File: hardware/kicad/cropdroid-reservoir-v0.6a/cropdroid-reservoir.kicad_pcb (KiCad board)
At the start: 2 copper layers, 303.3 x 178.1 mm, 42 parts, among them J1 703W-00_52, J10 PJ-102A, J11 PJ-102A, J12 PJ-102A, J13 PJ-102A, J14 PJ-102A, J2 2172034-1, J3 2172034-1, J4 PJ-102A, J5 3-213598-2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

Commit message: fix broken board edge
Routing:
- net Net-(J2-Pad1): track 217.5 -> 218.3 mm
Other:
- outline, holes or cut-outs redrawn
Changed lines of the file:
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@@
   (general
     (thickness 1.6)
-    (drawings 23)
-    (tracks 279)
+    (drawings 25)
+    (tracks 280)
     (zones 0)
     (modules 42)
@@
   )
   (setup
-    (last_trace_width 0.762)
+    (last_trace_width 0.254)
     (user_trace_width 0.254)
     (user_trace_width 0.762)
@@
       (padsonsilk false)
       (subtractmaskfromsilk false)
-      (outputformat 3)
+      (outputformat 5)
       (mirror false)
       (drillshape 0)
@@
     )
   )
+  (gr_line (start 155.5242 158.1658) (end 155.5242 163.7538) (layer Edge.Cuts) (width 0.05))
+  (gr_line (start 155.5242 163.7538) (end 155.5242 158.1658) (layer F.SilkS) (width 0.12))
   (gr_line (start 155.5242 163.7538) (end 155.5242 214.0458) (layer Edge.Cuts) (width 0.05))
-  (gr_line (start 64.3382 163.7538) (end 155.5242 163.7538) (layer Edge.Cuts) (width 0.05))
+  (gr_line (start 64.3382 158.1658) (end 155.5242 158.1658) (layer Edge.Cuts) (width 0.05))
   (gr_text "+5V DC" (at 307.4162 143.6878) (layer F.SilkS)
     (effects (font (size 1 1) (thickness 0.15)))
@@
     (effects (font (size 1 1) (thickness 0.15)))
   )
-  (gr_line (start 64.3382 35.9918) (end 64.3382 163.7538) (layer Edge.Cuts) (width 0.05))
+  (gr_line (start 64.3382 35.9918) (end 64.3382 158.1658) (layer Edge.Cuts) (width 0.05))
   (gr_text "+12v DC" (at 291.9222 176.1998) (layer F.SilkS)
     (effects (font (size 1 1) (thickness 0.15)))
@@
   (segment (start 320.3702 209.2198) (end 321.1322 208.4578) (width 0.254) (layer F.Cu) (net 79))
   (segment (start 149.3012 151.9428) (end 143.2052 151.9428) (width 0.254) (layer F.Cu) (net 80))
-  (segment (start 156.784284 159.425884) (end 149.3012 151.9428) (width 0.254) (layer F.Cu) (net 80))
-  (segment (start 156.784284 209.575574) (end 156.784284 159.425884) (width 0.254) (layer F.Cu) (net 80))
+  (segment (start 303.2 207.04) (end 296.85421 213.38579) (width 0.254) (layer F.Cu) (net 80))
+  (segment (start 156.784284 209.575574) (end 156.784284 157.901884) (width 0.254) (layer F.Cu) (net 80))
   (segment (start 160.5945 213.38579) (end 156.784284 209.575574) (width 0.254) (layer F.Cu) (net 80))
+  (segment (start 156.784284 157.901884) (end 150.8252 151.9428) (width 0.254) (layer F.Cu) (net 80))
   (segment (start 296.85421 213.38579) (end 160.5945 213.38579) (width 0.254) (layer F.Cu) (net 80))
-  (segment (start 296.85421 213.38579) (end 303.2 207.04) (width 0.254) (layer F.Cu) (net 80))
+  (segment (start 150.8252 151.9428) (end 149.3012 151.9428) (width 0.254) (layer F.Cu) (net 80))
   (zone (net 1) (net_name GND) (layer F.Cu) (hatch edge 0.508)
     (connect_pads (clearance 0.508))

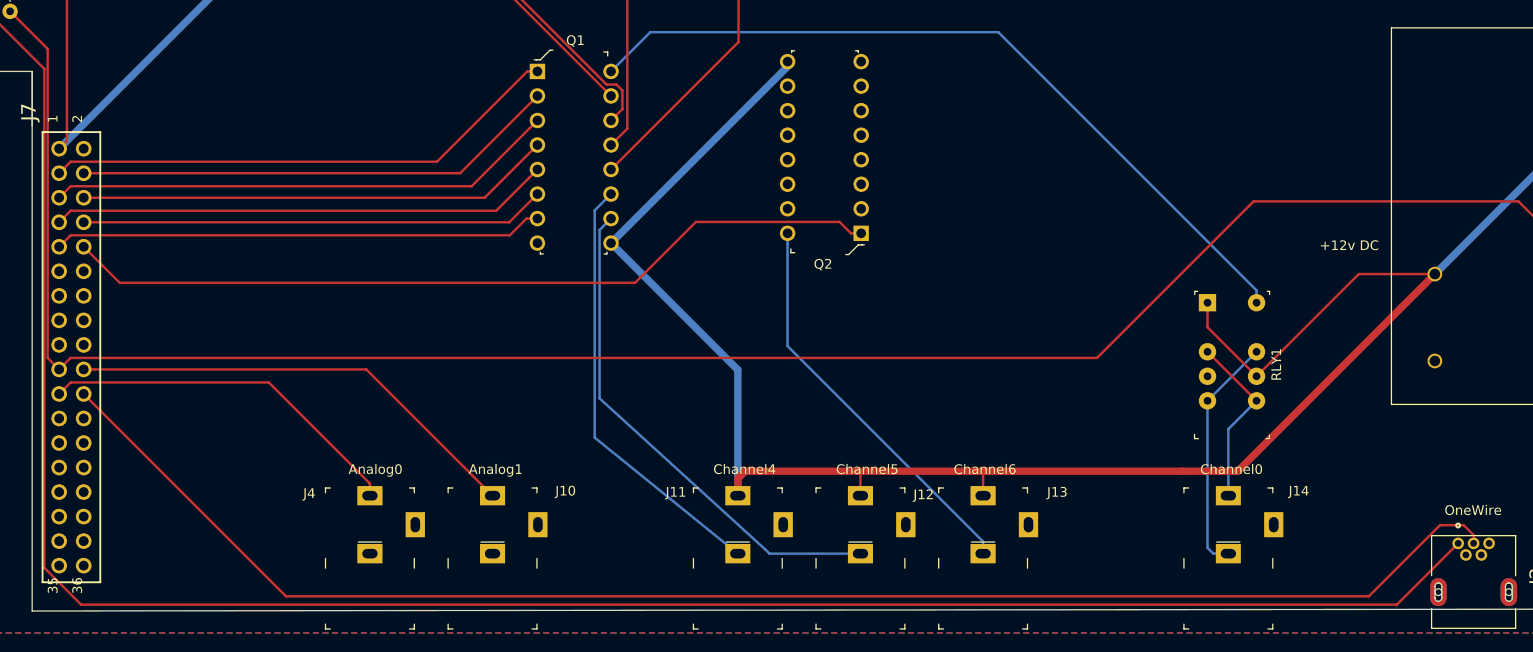
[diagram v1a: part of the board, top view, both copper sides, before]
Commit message: add board dimension drawings. space dc power jacks 3/4 in apart
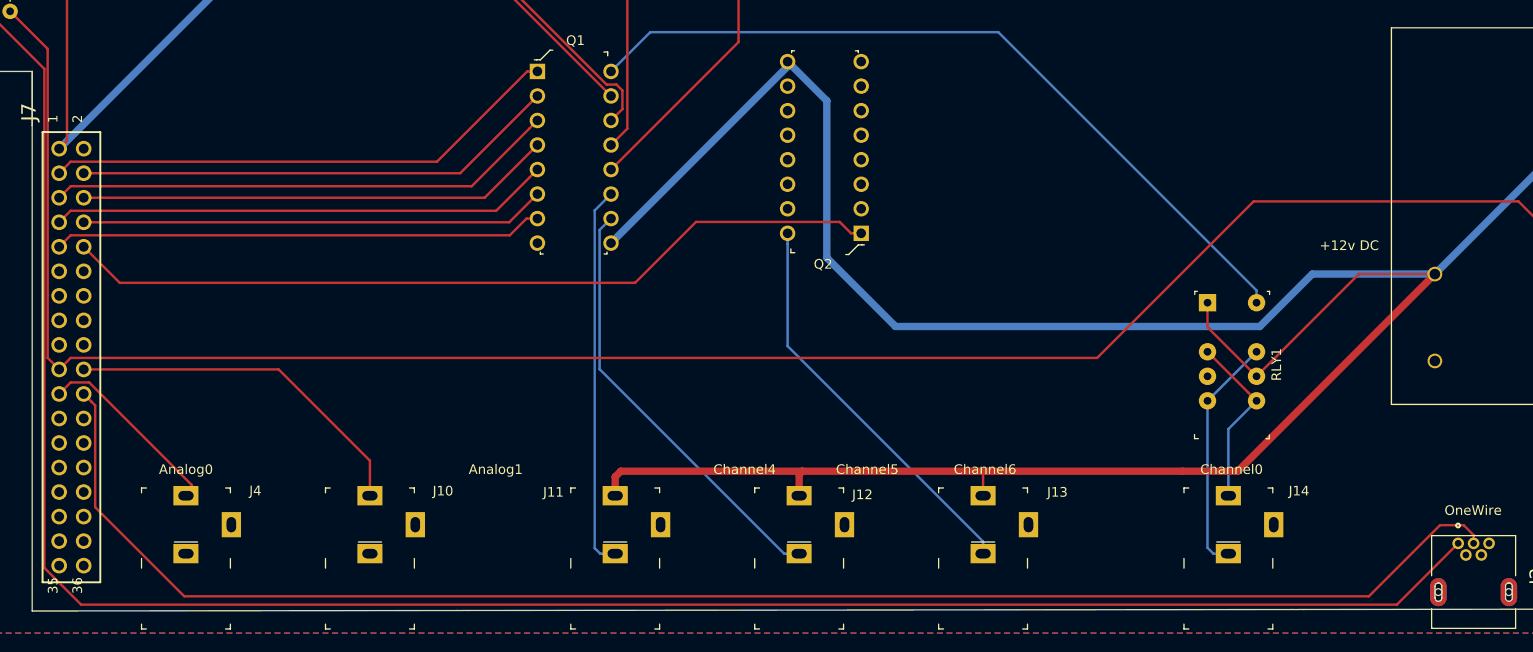
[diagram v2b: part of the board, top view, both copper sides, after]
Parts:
- moved J4 19.1 mm to (171.4, 205.1)
- moved J10 12.7 mm to (190.5, 205.1)
- moved J11 12.7 mm to (215.9, 205.1)
- moved J12 6.35 mm to (234.9, 205.1)
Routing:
- net Net-(D1-Pad1): track 576.6 -> 648.3 mm
- net Net-(J4-Pad1): track 38.3 -> 19.5 mm
- net Net-(J10-Pad1): track 47.8 -> 37.2 mm
- net Net-(J12-Pad2): track 52.4 -> 44.7 mm
- net Net-(J2-Pad3): track 157.0 -> 163.1 mm
- net Net-(J11-Pad2): track 45.0 -> 39.7 mm

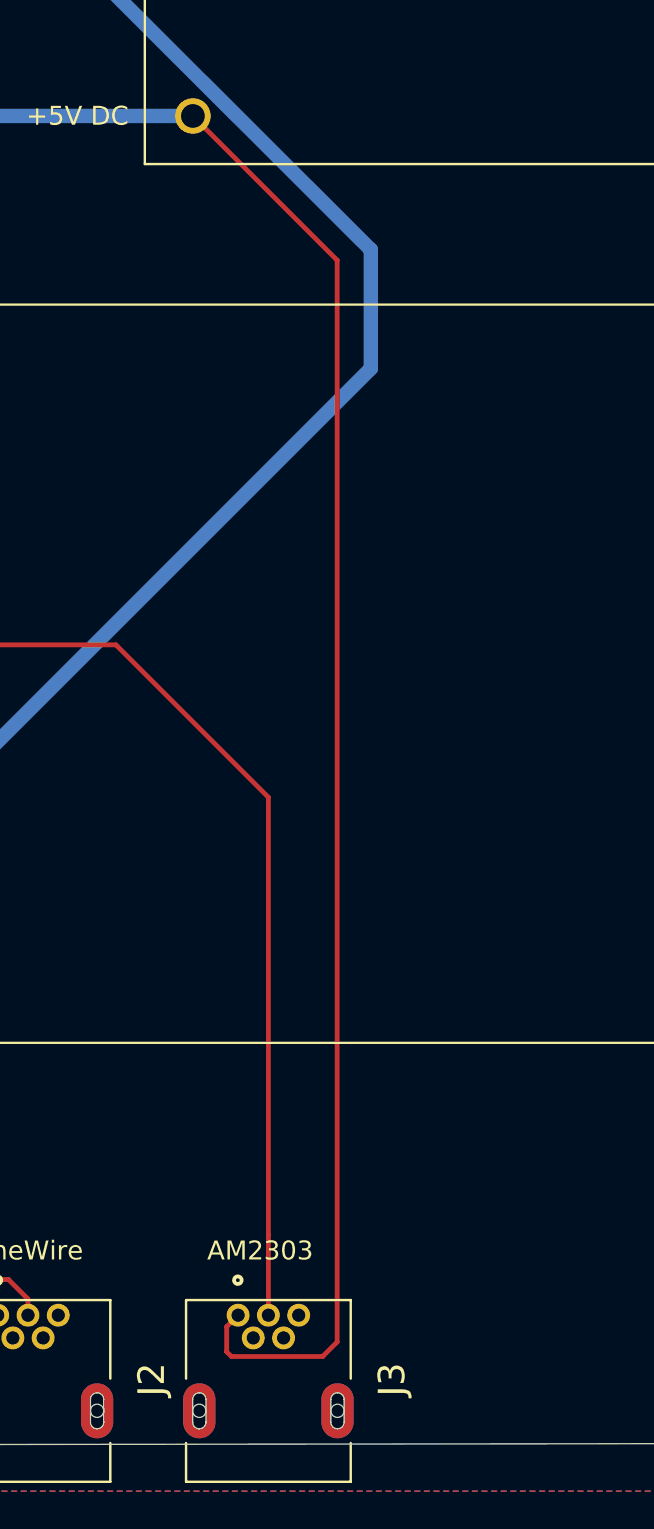
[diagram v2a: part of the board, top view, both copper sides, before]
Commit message: rename gerber folder to plots, generate final v0.6a artifacts for fab shop
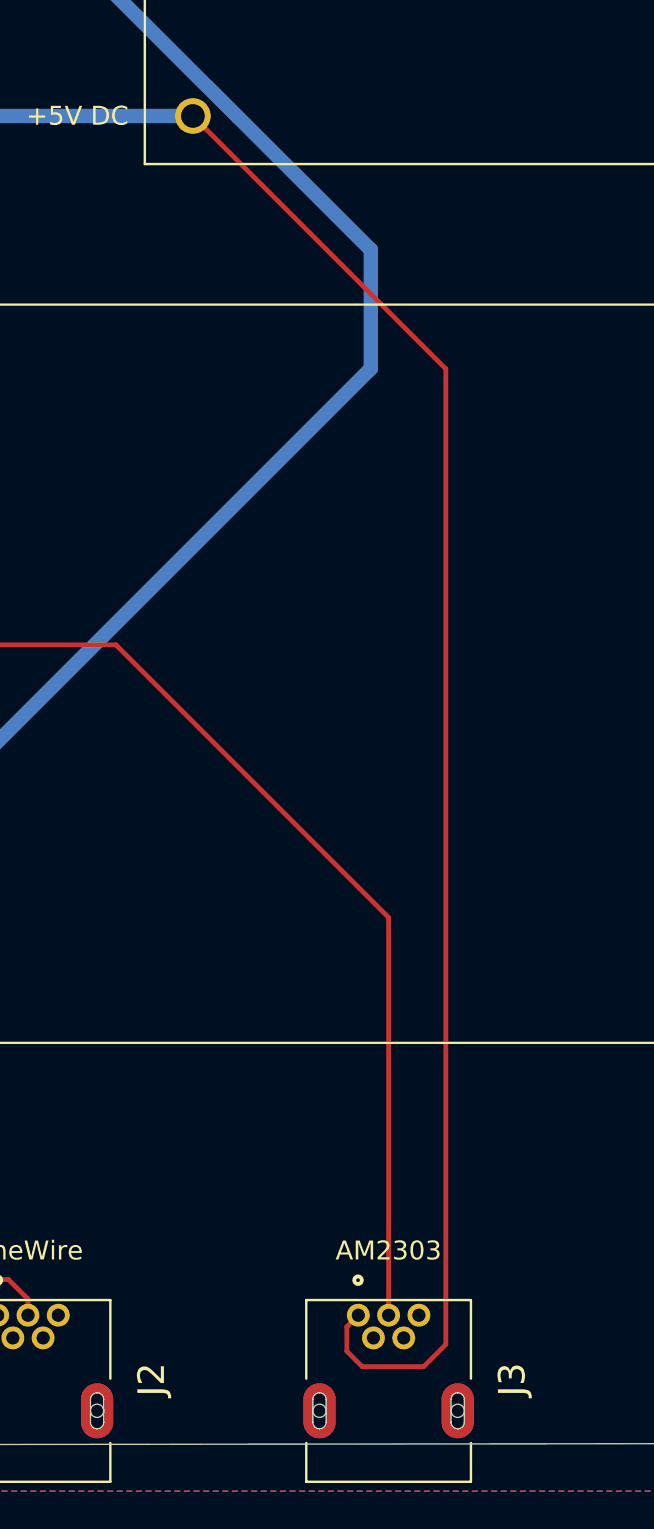
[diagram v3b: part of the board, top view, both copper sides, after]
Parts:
- moved J3 6.35 mm to (323.9, 212.1)
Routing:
- net Net-(J3-Pad3): track 236.3 -> 238.9 mm
- net Net-(J3-Pad1): track 282.5 -> 284.7 mm
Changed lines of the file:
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@@
     (thickness 1.6)
     (drawings 39)
-    (tracks 289)
+    (tracks 288)
     (zones 0)
     (modules 42)
@@
   )
   (setup
-    (last_trace_width 0.762)
+    (last_trace_width 0.254)
     (user_trace_width 0.254)
     (user_trace_width 0.762)
@@
       (padsonsilk false)
       (subtractmaskfromsilk false)
-      (outputformat 5)
+      (outputformat 1)
       (mirror false)
       (drillshape 0)
       (scaleselection 1)
-      (outputdirectory "gerber/"))
+      (outputdirectory "plots/"))
   )
   (net 0 "")
@@
   )
   (module 2172034-1:TE_2172034-1 (layer F.Cu)
-    (at 317.5 212.09 270)
+    (at 323.85 212.09 270)
     (fp_text reference J3 (at -1.65152 -6.52996 90) (layer F.SilkS)
       (effects (font (size 1.401276 1.401276) (thickness 0.015)))
@@
     (effects (font (size 1 1) (thickness 0.15)))
   )
-  (gr_text AM2303 (at 317.0682 203.6318) (layer F.SilkS)
+  (gr_text AM2303 (at 323.85 203.6318) (layer F.SilkS)
     (effects (font (size 1 1) (thickness 0.15)))
   )
@@
   (segment (start 157.127194 155.831794) (end 153.2382 151.9428) (width 0.254) (layer F.Cu) (net 34))
   (segment (start 157.127194 187.835794) (end 157.127194 155.831794) (width 0.254) (layer F.Cu) (net 34))
-  (segment (start 317.5 202.7936) (end 317.5 207.04) (width 0.254) (layer F.Cu) (net 34))
-  (segment (start 159.509206 187.835794) (end 265.808206 187.835794) (width 0.254) (layer F.Cu) (net 34))
-  (segment (start 158.3182 189.0268) (end 159.509206 187.835794) (width 0.254) (layer F.Cu) (net 34))
+  (segment (start 323.85 186.0296) (end 323.85 207.04) (width 0.254) (layer F.Cu) (net 34))
+  (segment (start 309.4482 171.6278) (end 323.85 186.0296) (width 0.254) (layer F.Cu) (net 34))
   (segment (start 265.808206 187.835794) (end 282.0162 171.6278) (width 0.254) (layer F.Cu) (net 34))
+  (segment (start 158.3182 189.0268) (end 159.509206 187.835794) (width 0.254) (layer F.Cu) (net 34))
   (segment (start 282.0162 171.6278) (end 309.4482 171.6278) (width 0.254) (layer F.Cu) (net 34))
-  (segment (start 309.4482 171.6278) (end 317.5 179.6796) (width 0.254) (layer F.Cu) (net 34))
-  (segment (start 317.5 179.6796) (end 317.5 202.7936) (width 0.254) (layer F.Cu) (net 34))
+  (segment (start 159.509206 187.835794) (end 265.808206 187.835794) (width 0.254) (layer F.Cu) (net 34))
   (segment (start 158.3182 191.5668) (end 159.509206 190.375794) (width 0.254) (layer F.Cu) (net 35))
   (segment (start 172.0342 201.5208) (end 171.782417 201.772583) (width 0.254) (layer F.Cu) (net 35))
@@
   (segment (start 156.3497 144.8943) (end 146.3167 144.8943) (width 0.254) (layer F.Cu) (net 79))
   (segment (start 159.128204 147.672804) (end 156.3497 144.8943) (width 0.254) (layer F.Cu) (net 79))
-  (segment (start 315.296001 207.643999) (end 315.296001 208.971601) (width 0.254) (layer F.Cu) (net 79))
-  (segment (start 315.9 207.04) (end 315.296001 207.643999) (width 0.254) (layer F.Cu) (net 79))
-  (segment (start 315.296001 208.971601) (end 315.5442 209.2198) (width 0.254) (layer F.Cu) (net 79))
-  (segment (start 321.1322 151.3078) (end 313.5122 143.6878) (width 0.254) (layer F.Cu) (net 79))
-  (segment (start 321.1322 208.4578) (end 321.1322 151.3078) (width 0.254) (layer F.Cu) (net 79))
-  (segment (start 315.5442 209.2198) (end 320.3702 209.2198) (width 0.254) (layer F.Cu) (net 79))
-  (segment (start 320.3702 209.2198) (end 321.1322 208.4578) (width 0.254) (layer F.Cu) (net 79))
+  (segment (start 321.646001 207.643999) (end 321.646001 208.946201) (width 0.254) (layer F.Cu) (net 79))
+  (segment (start 322.25 207.04) (end 321.646001 207.643999) (width 0.254) (layer F.Cu) (net 79))
+  (segment (start 321.646001 208.946201) (end 322.453 209.7532) (width 0.254) (layer F.Cu) (net 79))
+  (segment (start 322.453 209.7532) (end 325.7042 209.7532) (width 0.254) (layer F.Cu) (net 79))
+  (segment (start 325.7042 209.7532) (end 326.8726 208.5848) (width 0.254) (layer F.Cu) (net 79))
+  (segment (start 326.8726 157.0482) (end 313.5122 143.6878) (width 0.254) (layer F.Cu) (net 79))
+  (segment (start 326.8726 208.5848) (end 326.8726 157.0482) (width 0.254) (layer F.Cu) (net 79))
   (segment (start 149.3012 151.9428) (end 143.2052 151.9428) (width 0.254) (layer F.Cu) (net 80))
   (segment (start 303.2 207.04) (end 296.85421 213.38579) (width 0.254) (layer F.Cu) (net 80))

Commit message: add /sys endpoint
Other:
- board text added: "Channel7"
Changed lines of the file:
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@@
   (general
     (thickness 1.6)
-    (drawings 39)
+    (drawings 40)
     (tracks 288)
     (zones 0)
@@
     )
   )
+  (gr_text Channel4 (at 261.9502 90.8685 90) (layer F.SilkS)
+    (effects (font (size 1 1) (thickness 0.15)))
+  )
   (dimension 63.5 (width 0.15) (layer Dwgs.User)
     (gr_text "2.5000 in" (at 307.8942 67.7418 90) (layer Dwgs.User)
@@
     (effects (font (size 1 1) (thickness 0.15)))
   )
-  (gr_text Channel6 (at 254.2032 199.39) (layer F.SilkS)
+  (gr_text Channel7 (at 254.2032 199.39) (layer F.SilkS)
     (effects (font (size 1 1) (thickness 0.15)))
   )
-  (gr_text Channel5 (at 242.0112 199.39) (layer F.SilkS)
+  (gr_text Channel6 (at 234.95 199.39) (layer F.SilkS)
     (effects (font (size 1 1) (thickness 0.15)))
   )
-  (gr_text Channel4 (at 229.3112 199.39) (layer F.SilkS)
+  (gr_text Channel5 (at 215.9 199.39) (layer F.SilkS)
     (effects (font (size 1 1) (thickness 0.15)))
   )
@@
     (effects (font (size 1 1) (thickness 0.15)))
   )
-  (gr_text Analog1 (at 203.5302 199.39) (layer F.SilkS)
+  (gr_text Analog1 (at 190.5 199.39) (layer F.SilkS)
     (effects (font (size 1 1) (thickness 0.15)))
   )
